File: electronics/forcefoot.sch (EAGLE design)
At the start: 60 parts

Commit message: Tying AGND to GND
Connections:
- removed net AGND$1: C2.1, HX1.AGND, R17.1
- removed net AGND$2: C6.1, HX2.AGND, R5.1
- removed net AGND$3: C10.1, HX3.AGND, R8.1
- removed net AGND$4: C14.1, HX4.AGND, R11.1
- net GND: now also C10.1, C14.1, C2.1, C6.1, HX1.AGND, HX2.AGND, HX3.AGND, HX4.AGND, R11.1, R17.1, R5.1, R8.1
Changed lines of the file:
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@@
 <part name="GND7" library="supply1" deviceset="GND" device=""/>
 <part name="GND8" library="supply1" deviceset="GND" device=""/>
+<part name="GND9" library="supply1" deviceset="GND" device=""/>
+<part name="GND10" library="supply1" deviceset="GND" device=""/>
+<part name="GND12" library="supply1" deviceset="GND" device=""/>
+<part name="GND13" library="supply1" deviceset="GND" device=""/>
 </parts>
 <sheets>
@@
 <instance part="GND7" gate="1" x="190.5" y="132.08"/>
 <instance part="GND8" gate="1" x="200.66" y="132.08"/>
+<instance part="GND9" gate="1" x="25.4" y="30.48"/>
+<instance part="GND10" gate="1" x="144.78" y="27.94"/>
+<instance part="GND12" gate="1" x="264.16" y="27.94"/>
+<instance part="GND13" gate="1" x="378.46" y="27.94"/>
 </instances>
 <busses>
@@
 <pinref part="U$4" gate="G$1" pin="-"/>
 <wire x1="200.66" y1="137.16" x2="200.66" y2="134.62" width="0.1524" layer="91"/>
+</segment>
+<segment>
+<pinref part="C2" gate="G$1" pin="1"/>
+<wire x1="45.72" y1="53.34" x2="43.18" y2="53.34" width="0.1524" layer="91"/>
+<wire x1="43.18" y1="33.02" x2="43.18" y2="53.34" width="0.1524" layer="91"/>
+<wire x1="43.18" y1="53.34" x2="43.18" y2="58.42" width="0.1524" layer="91"/>
+<pinref part="HX1" gate="G$1" pin="AGND"/>
+<wire x1="43.18" y1="58.42" x2="55.88" y2="58.42" width="0.1524" layer="91"/>
+<pinref part="R17" gate="G$1" pin="1"/>
+<wire x1="25.4" y1="35.56" x2="25.4" y2="33.02" width="0.1524" layer="91"/>
+<wire x1="25.4" y1="33.02" x2="43.18" y2="33.02" width="0.1524" layer="91"/>
+<junction x="25.4" y="33.02"/>
+<junction x="43.18" y="33.02"/>
+<junction x="43.18" y="53.34"/>
+<pinref part="GND9" gate="1" pin="GND"/>
+</segment>
+<segment>
+<pinref part="R5" gate="G$1" pin="1"/>
+<wire x1="144.78" y1="33.02" x2="144.78" y2="30.48" width="0.1524" layer="91"/>
+<pinref part="C6" gate="G$1" pin="1"/>
+<wire x1="165.1" y1="50.8" x2="162.56" y2="50.8" width="0.1524" layer="91"/>
+<wire x1="144.78" y1="30.48" x2="162.56" y2="30.48" width="0.1524" layer="91"/>
+<wire x1="162.56" y1="30.48" x2="162.56" y2="50.8" width="0.1524" layer="91"/>
+<wire x1="162.56" y1="50.8" x2="162.56" y2="55.88" width="0.1524" layer="91"/>
+<pinref part="HX2" gate="G$1" pin="AGND"/>
+<wire x1="162.56" y1="55.88" x2="175.26" y2="55.88" width="0.1524" layer="91"/>
+<junction x="162.56" y="50.8"/>
+<pinref part="GND10" gate="1" pin="GND"/>
+<junction x="144.78" y="30.48"/>
+</segment>
+<segment>
+<pinref part="R8" gate="G$1" pin="1"/>
+<wire x1="264.16" y1="33.02" x2="264.16" y2="30.48" width="0.1524" layer="91"/>
+<pinref part="C10" gate="G$1" pin="1"/>
+<wire x1="284.48" y1="50.8" x2="281.94" y2="50.8" width="0.1524" layer="91"/>
+<wire x1="264.16" y1="30.48" x2="281.94" y2="30.48" width="0.1524" layer="91"/>
+<wire x1="281.94" y1="30.48" x2="281.94" y2="50.8" width="0.1524" layer="91"/>
+<wire x1="281.94" y1="50.8" x2="281.94" y2="55.88" width="0.1524" layer="91"/>
+<pinref part="HX3" gate="G$1" pin="AGND"/>
+<wire x1="281.94" y1="55.88" x2="294.64" y2="55.88" width="0.1524" layer="91"/>
+<junction x="281.94" y="50.8"/>
+<pinref part="GND12" gate="1" pin="GND"/>
+<junction x="264.16" y="30.48"/>
+</segment>
+<segment>
+<pinref part="R11" gate="G$1" pin="1"/>
+<wire x1="378.46" y1="33.02" x2="378.46" y2="30.48" width="0.1524" layer="91"/>
+<pinref part="C14" gate="G$1" pin="1"/>
+<wire x1="398.78" y1="50.8" x2="396.24" y2="50.8" width="0.1524" layer="91"/>
+<wire x1="378.46" y1="30.48" x2="396.24" y2="30.48" width="0.1524" layer="91"/>
+<wire x1="396.24" y1="30.48" x2="396.24" y2="50.8" width="0.1524" layer="91"/>
+<wire x1="396.24" y1="50.8" x2="396.24" y2="55.88" width="0.1524" layer="91"/>
+<pinref part="HX4" gate="G$1" pin="AGND"/>
+<wire x1="396.24" y1="55.88" x2="408.94" y2="55.88" width="0.1524" layer="91"/>
+<junction x="396.24" y="50.8"/>
+<pinref part="GND13" gate="1" pin="GND"/>
+<junction x="378.46" y="30.48"/>
 </segment>
 </net>
@@
 </segment>
 </net>
-<net name="AGND$1" class="0">
-<segment>
-<pinref part="C2" gate="G$1" pin="1"/>
-<wire x1="45.72" y1="53.34" x2="43.18" y2="53.34" width="0.1524" layer="91"/>
-<wire x1="43.18" y1="33.02" x2="43.18" y2="53.34" width="0.1524" layer="91"/>
-<wire x1="43.18" y1="53.34" x2="43.18" y2="58.42" width="0.1524" layer="91"/>
-<pinref part="HX1" gate="G$1" pin="AGND"/>
-<wire x1="43.18" y1="58.42" x2="55.88" y2="58.42" width="0.1524" layer="91"/>
-<pinref part="R17" gate="G$1" pin="1"/>
-<wire x1="25.4" y1="35.56" x2="25.4" y2="33.02" width="0.1524" layer="91"/>
-<wire x1="25.4" y1="33.02" x2="43.18" y2="33.02" width="0.1524" layer="91"/>
-<junction x="25.4" y="33.02"/>
-<junction x="43.18" y="33.02"/>
-<junction x="43.18" y="53.34"/>
-</segment>
-</net>
 <net name="N$3" class="0">
 <segment>
@@
 </segment>
 </net>
-<net name="AGND$2" class="0">
-<segment>
-<pinref part="R5" gate="G$1" pin="1"/>
-<wire x1="144.78" y1="33.02" x2="144.78" y2="30.48" width="0.1524" layer="91"/>
-<pinref part="C6" gate="G$1" pin="1"/>
-<wire x1="165.1" y1="50.8" x2="162.56" y2="50.8" width="0.1524" layer="91"/>
-<wire x1="144.78" y1="30.48" x2="162.56" y2="30.48" width="0.1524" layer="91"/>
-<wire x1="162.56" y1="30.48" x2="162.56" y2="50.8" width="0.1524" layer="91"/>
-<wire x1="162.56" y1="50.8" x2="162.56" y2="55.88" width="0.1524" layer="91"/>
-<pinref part="HX2" gate="G$1" pin="AGND"/>
-<wire x1="162.56" y1="55.88" x2="175.26" y2="55.88" width="0.1524" layer="91"/>
-<junction x="162.56" y="50.8"/>
-</segment>
-</net>
 <net name="N$4" class="0">
 <segment>
@@
 </segment>
 </net>
-<net name="AGND$3" class="0">
-<segment>
-<pinref part="R8" gate="G$1" pin="1"/>
-<wire x1="264.16" y1="33.02" x2="264.16" y2="30.48" width="0.1524" layer="91"/>
-<pinref part="C10" gate="G$1" pin="1"/>
-<wire x1="284.48" y1="50.8" x2="281.94" y2="50.8" width="0.1524" layer="91"/>
-<wire x1="264.16" y1="30.48" x2="281.94" y2="30.48" width="0.1524" layer="91"/>
-<wire x1="281.94" y1="30.48" x2="281.94" y2="50.8" width="0.1524" layer="91"/>
-<wire x1="281.94" y1="50.8" x2="281.94" y2="55.88" width="0.1524" layer="91"/>
-<pinref part="HX3" gate="G$1" pin="AGND"/>
-<wire x1="281.94" y1="55.88" x2="294.64" y2="55.88" width="0.1524" layer="91"/>
-<junction x="281.94" y="50.8"/>
-</segment>
-</net>
 <net name="N$6" class="0">
 <segment>
@@
 </segment>
 </net>
-<net name="AGND$4" class="0">
-<segment>
-<pinref part="R11" gate="G$1" pin="1"/>
-<wire x1="378.46" y1="33.02" x2="378.46" y2="30.48" width="0.1524" layer="91"/>
-<pinref part="C14" gate="G$1" pin="1"/>
-<wire x1="398.78" y1="50.8" x2="396.24" y2="50.8" width="0.1524" layer="91"/>
-<wire x1="378.46" y1="30.48" x2="396.24" y2="30.48" width="0.1524" layer="91"/>
-<wire x1="396.24" y1="30.48" x2="396.24" y2="50.8" width="0.1524" layer="91"/>
-<wire x1="396.24" y1="50.8" x2="396.24" y2="55.88" width="0.1524" layer="91"/>
-<pinref part="HX4" gate="G$1" pin="AGND"/>
-<wire x1="396.24" y1="55.88" x2="408.94" y2="55.88" width="0.1524" layer="91"/>
-<junction x="396.24" y="50.8"/>
-</segment>
-</net>

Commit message: Tweaking for v2
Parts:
- removed DXL: CONNEC_1X04, rhoban:CONNEC_1X04
- removed IC1: (no value), SparkFun-PowerIC:V_REG_78XX-TO-220
- removed MAPLE_MINI: MAPLE_MINI, rhoban:MAPLE_MINI
- added C17, C18: 22, rhoban:C_EU_22PF
- added R27: 10k, SparkFun-Passives:RESISTOR0805-RES
- added R28, R29: 3K, SparkFun-Passives:RESISTOR0805-RES
- added U$17: GY-85, rhoban:GY-85
- added U$28: CONNEC_2X03, rhoban:CONNEC_2X03
- added U$5: REG_5V, rhoban:REG_5V
- added U$8: CONNEC_1X04_485, rhoban:CONNEC_1X04_485
- added U2: ATMEGA168, SparkFun-DigitalIC:ATMEGA168
- added XTAL1: QUARTZ, rhoban:QUARTZ
- U$10, U$13, U$3, U$7: value CONNEC_1X04 -> CONNEC_1X041.5; device rhoban:CONNEC_1X04 -> rhoban:CONNEC_1X041.5
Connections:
- new net 3.3: R28.2, R29.2, U$17.3.3
- new net IMU_SCL: R28.1, U$17.SCL, U2.PC5(ADC5/SCL)
- new net IMU_SDA: R29.1, U$17.SDA, U2.PC4(ADC4/SDA)
- new net MISO: U$28.1, U2.PB4(MISO)
- new net MOSI: U$28.4, U2.PB3(MOSI/OC2)
- new net N$19: C17.2, U2.PB6(XTAL1/TOSC1), XTAL1.2
- new net N$20: C18.2, U2.PB7(XTAL2/TOSC2), XTAL1.1
- new net RESET: R27.1, U$28.5, U2.PC6(/RESET)
- new net SCK: U$28.3, U2.PB5(SCK)
- net DIRECTION: now also U2.PD2(INT0); no longer MAPLE_MINI.2
- net DOUT1: now also U2.PC1(ADC1); no longer MAPLE_MINI.16
- net DOUT2: now also U2.PC3(ADC3); no longer MAPLE_MINI.18
- net DOUT3: now also U2.PD4(XCK/T0); no longer MAPLE_MINI.20
- net DOUT4: now also U2.ADC7; no longer MAPLE_MINI.22
- net GND: now also C17.1, C18.1, U$17.GND, U$28.6, U$5.GND, U$8.1, U2.AGND, U2.GND@1, U2.GND@2; no longer DXL.1, IC1.GND, MAPLE_MINI.GND
- net RS+: now also U$8.3; no longer DXL.3
- net RS-: now also U$8.4; no longer DXL.4
- net RX: now also U2.PD0(RXD); no longer MAPLE_MINI.0
- net SCK1: now also U2.PC0(ADC0); no longer MAPLE_MINI.15
- net SCK2: now also U2.PC2(ADC2); no longer MAPLE_MINI.17
- net SCK3: now also U2.PD3(INT1); no longer MAPLE_MINI.19
- net SCK4: now also U2.ADC6; no longer MAPLE_MINI.21
- net TX: now also U2.PD1(TXD); no longer MAPLE_MINI.1
- net VCC: now also U$17.VCC_IN, U$5.OUT; no longer IC1.OUT, MAPLE_MINI.VIN
- net VIN: now also R27.2, U$28.2, U$5.IN, U$8.2, U2.AREF, U2.VCC@1, U2.VCC@2; no longer DXL.2, IC1.IN
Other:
- moved on the sheet: MAX485, R1, R13, R14, R15, R18, R2, U$2, U$4

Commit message: Fixing r value
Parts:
- R14, R15: value 3k -> 22
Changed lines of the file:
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@@
 <part name="GND2" library="supply1" deviceset="GND" device=""/>
 <part name="P+1" library="supply1" deviceset="VCC" device=""/>
-<part name="R14" library="rhoban" deviceset="RESISTANCE" device="-R0805" value="3k"/>
-<part name="R15" library="rhoban" deviceset="RESISTANCE" device="-R0805" value="3k"/>
+<part name="R14" library="rhoban" deviceset="RESISTANCE" device="-R0805" value="22"/>
+<part name="R15" library="rhoban" deviceset="RESISTANCE" device="-R0805" value="22"/>
 <part name="R19" library="SparkFun-Passives" deviceset="RESISTOR" device="0805-RES" value="3K"/>
 <part name="R20" library="SparkFun-Passives" deviceset="RESISTOR" device="0805-RES" value="3K"/>

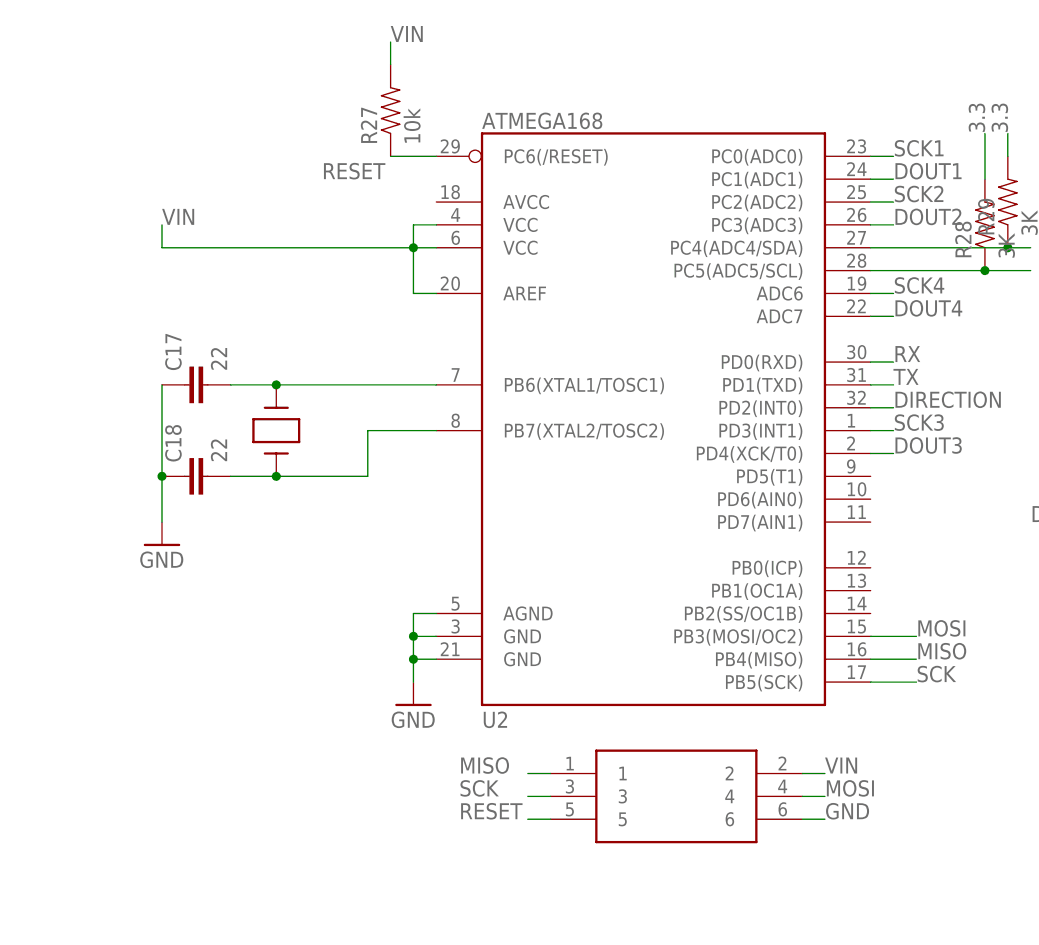
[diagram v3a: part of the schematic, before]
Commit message: Fixing vin -> vcc for mcu
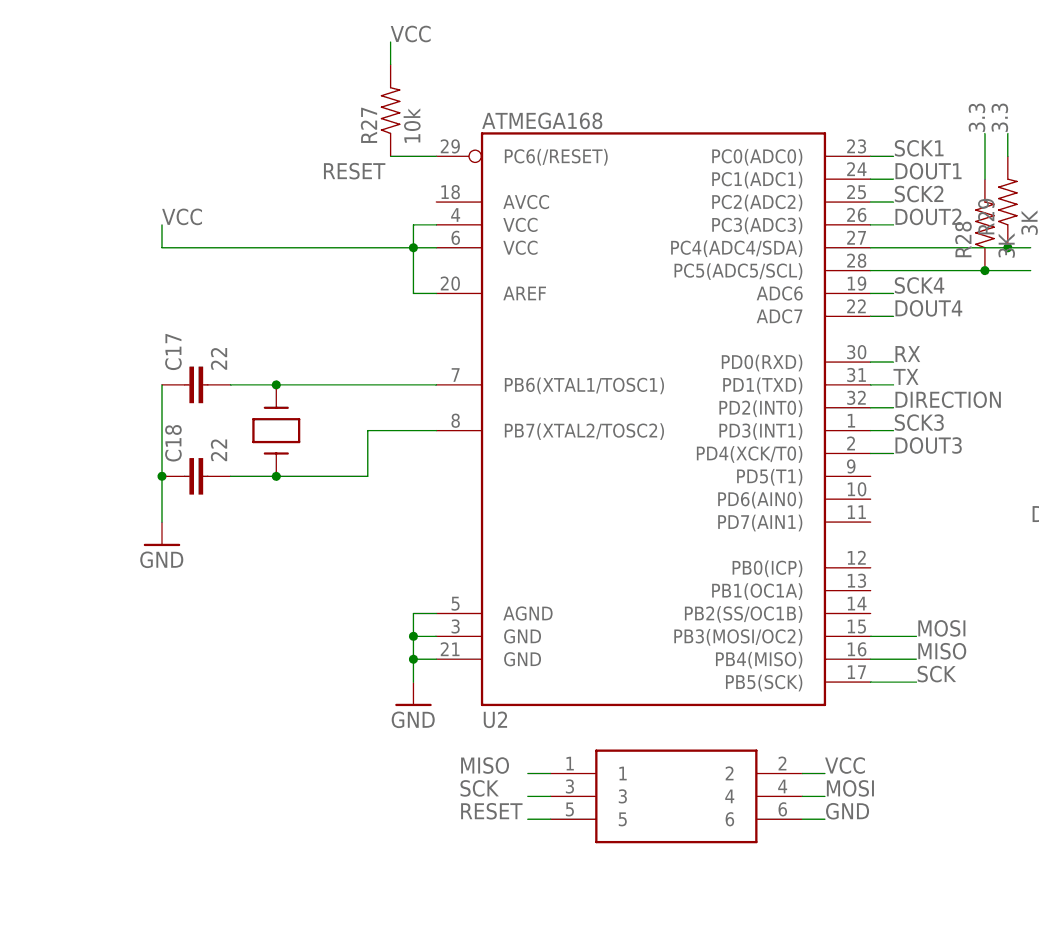
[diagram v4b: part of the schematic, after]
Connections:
- net VCC: now also R27.2, U$28.2, U2.AREF, U2.VCC@1, U2.VCC@2
- net VIN: no longer R27.2, U$28.2, U2.AREF, U2.VCC@1, U2.VCC@2
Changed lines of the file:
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@@
 <label x="226.06" y="187.96" size="1.778" layer="95"/>
+</segment>
+<segment>
+<wire x1="119.38" y1="167.64" x2="119.38" y2="165.1" width="0.1524" layer="91"/>
+<wire x1="119.38" y1="165.1" x2="147.32" y2="165.1" width="0.1524" layer="91"/>
+<wire x1="147.32" y1="165.1" x2="149.86" y2="165.1" width="0.1524" layer="91"/>
+<wire x1="149.86" y1="167.64" x2="147.32" y2="167.64" width="0.1524" layer="91"/>
+<wire x1="147.32" y1="167.64" x2="147.32" y2="165.1" width="0.1524" layer="91"/>
+<junction x="147.32" y="165.1"/>
+<wire x1="149.86" y1="160.02" x2="147.32" y2="160.02" width="0.1524" layer="91"/>
+<wire x1="147.32" y1="160.02" x2="147.32" y2="165.1" width="0.1524" layer="91"/>
+<label x="119.38" y="167.64" size="1.778" layer="95"/>
+<pinref part="U2" gate="G$1" pin="VCC@1"/>
+<pinref part="U2" gate="G$1" pin="VCC@2"/>
+<pinref part="U2" gate="G$1" pin="AREF"/>
+</segment>
+<segment>
+<pinref part="U$28" gate="G$1" pin="2"/>
+<wire x1="190.5" y1="106.68" x2="193.04" y2="106.68" width="0.1524" layer="91"/>
+<label x="193.04" y="106.68" size="1.778" layer="95"/>
+</segment>
+<segment>
+<wire x1="144.78" y1="187.96" x2="144.78" y2="185.42" width="0.1524" layer="91"/>
+<pinref part="R27" gate="G$1" pin="2"/>
+<label x="144.78" y="187.96" size="1.778" layer="95"/>
 </segment>
 </net>
@@
 </segment>
 <segment>
-<pinref part="U$28" gate="G$1" pin="2"/>
-<wire x1="190.5" y1="106.68" x2="193.04" y2="106.68" width="0.1524" layer="91"/>
-<label x="193.04" y="106.68" size="1.778" layer="95"/>
-</segment>
-<segment>
-<wire x1="119.38" y1="167.64" x2="119.38" y2="165.1" width="0.1524" layer="91"/>
-<wire x1="119.38" y1="165.1" x2="147.32" y2="165.1" width="0.1524" layer="91"/>
-<wire x1="147.32" y1="165.1" x2="149.86" y2="165.1" width="0.1524" layer="91"/>
-<wire x1="149.86" y1="167.64" x2="147.32" y2="167.64" width="0.1524" layer="91"/>
-<wire x1="147.32" y1="167.64" x2="147.32" y2="165.1" width="0.1524" layer="91"/>
-<junction x="147.32" y="165.1"/>
-<wire x1="149.86" y1="160.02" x2="147.32" y2="160.02" width="0.1524" layer="91"/>
-<wire x1="147.32" y1="160.02" x2="147.32" y2="165.1" width="0.1524" layer="91"/>
-<label x="119.38" y="167.64" size="1.778" layer="95"/>
-<pinref part="U2" gate="G$1" pin="VCC@1"/>
-<pinref part="U2" gate="G$1" pin="VCC@2"/>
-<pinref part="U2" gate="G$1" pin="AREF"/>
-</segment>
-<segment>
-<wire x1="144.78" y1="187.96" x2="144.78" y2="185.42" width="0.1524" layer="91"/>
-<pinref part="R27" gate="G$1" pin="2"/>
-<label x="144.78" y="187.96" size="1.778" layer="95"/>
-</segment>
-<segment>

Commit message: Fixing connections
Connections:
- removed net 1A-1: R21.1, R22.2
- removed net 1A-2: R23.1, R24.2
- removed net 1A-3: R25.1, R26.2
- net 2A-: now also R21.1, R22.2
- net 3A-: now also R23.1, R24.2
- net 4A-: now also R25.1, R26.2
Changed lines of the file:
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@@
 <junction x="165.1" y="25.4"/>
+</segment>
+<segment>
+<wire x1="144.78" y1="25.4" x2="127" y2="25.4" width="0.1524" layer="91"/>
+<pinref part="R21" gate="G$1" pin="1"/>
+<pinref part="R22" gate="G$1" pin="2"/>
+<junction x="127" y="25.4"/>
 </segment>
 </net>
@@
 <junction x="398.78" y="25.4"/>
 </segment>
+<segment>
+<wire x1="378.46" y1="25.4" x2="360.68" y2="25.4" width="0.1524" layer="91"/>
+<pinref part="R25" gate="G$1" pin="1"/>
+<pinref part="R26" gate="G$1" pin="2"/>
+<junction x="360.68" y="25.4"/>
+</segment>
 </net>
 <net name="3A-" class="0">
@@
 <wire x1="264.16" y1="15.24" x2="264.16" y2="25.4" width="0.1524" layer="91"/>
 <junction x="284.48" y="25.4"/>
+</segment>
+<segment>
+<wire x1="264.16" y1="25.4" x2="246.38" y2="25.4" width="0.1524" layer="91"/>
+<pinref part="R23" gate="G$1" pin="1"/>
+<pinref part="R24" gate="G$1" pin="2"/>
+<junction x="246.38" y="25.4"/>
 </segment>
 </net>
@@
 </segment>
 </net>
-<net name="1A-1" class="0">
-<segment>
-<wire x1="144.78" y1="25.4" x2="127" y2="25.4" width="0.1524" layer="91"/>
-<pinref part="R21" gate="G$1" pin="1"/>
-<pinref part="R22" gate="G$1" pin="2"/>
-<junction x="127" y="25.4"/>
-</segment>
-</net>
-<net name="1A-2" class="0">
-<segment>
-<wire x1="264.16" y1="25.4" x2="246.38" y2="25.4" width="0.1524" layer="91"/>
-<pinref part="R23" gate="G$1" pin="1"/>
-<pinref part="R24" gate="G$1" pin="2"/>
-<junction x="246.38" y="25.4"/>
-</segment>
-</net>
-<net name="1A-3" class="0">
-<segment>
-<wire x1="378.46" y1="25.4" x2="360.68" y2="25.4" width="0.1524" layer="91"/>
-<pinref part="R25" gate="G$1" pin="1"/>
-<pinref part="R26" gate="G$1" pin="2"/>
-<junction x="360.68" y="25.4"/>
-</segment>
-</net>

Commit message: Improving names and silk
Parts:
- removed U$17: GY-85, rhoban:GY-85
- removed U$28: CONNEC_2X03, rhoban:CONNEC_2X03
- removed U$5: REG_5V, rhoban:REG_5V
- removed U$8: CONNEC_1X04_485, rhoban:CONNEC_1X04_485
- added DXL: CONNEC_1X04_485, rhoban:CONNEC_1X04_485
- added IMU: GY-85, rhoban:GY-85
- added ISP: CONNEC_2X03, rhoban:CONNEC_2X03
- added REG: REG_5V, rhoban:REG_5V
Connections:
- net 3.3: now also IMU.3.3; no longer U$17.3.3
- net GND: now also DXL.1, IMU.GND, ISP.6, REG.GND; no longer U$17.GND, U$28.6, U$5.GND, U$8.1
- net IMU_SCL: now also IMU.SCL; no longer U$17.SCL
- net IMU_SDA: now also IMU.SDA; no longer U$17.SDA
- net MISO: now also ISP.1; no longer U$28.1
- net MOSI: now also ISP.4; no longer U$28.4
- net RESET: now also ISP.5; no longer U$28.5
- net RS+: now also DXL.3; no longer U$8.3
- net RS-: now also DXL.4; no longer U$8.4
- net SCK: now also ISP.3; no longer U$28.3
- net VCC: now also IMU.VCC_IN, ISP.2, REG.OUT; no longer U$17.VCC_IN, U$28.2, U$5.OUT
- net VIN: now also DXL.2, REG.IN; no longer U$5.IN, U$8.2
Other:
- moved on the sheet: C17, C18, MAX485, R1, R13, R14, R15, R18, R2, R27, R28, R29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

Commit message: Adding FARNELL attributes and writing BOM
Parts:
- C1, C10, C11, C13, C14, C15, C2, C3, C5, C6, C7, C9: FARNELL (none) -> 2525136RL
- C12, C16, C4, C8: FARNELL (none) -> 2688486RL
- C17, C18: FARNELL (none) -> 1759489RL
- DXL: FARNELL (none) -> 1104204 OR 9979620
- HX1, HX2, HX3, HX4: FARNELL (none) -> HX711
- IMU: FARNELL (none) -> -
- ISP: FARNELL (none) -> 1593440
- MAX485: FARNELL (none) -> 1564306
- R1, R13, R18, R19, R2, R20, R21, R22, R23, R24, R25, R26, R28, R29: FARNELL (none) -> 2074431
- R10, R16, R4, R7: FARNELL (none) -> 2074395
- R11, R17, R5, R8: FARNELL (none) -> 2074518
- R12, R3, R6, R9: FARNELL (none) -> 2074332RL
- R14, R15: FARNELL (none) -> 2446926
- R27: FARNELL (none) -> 2074334RL
- REG: FARNELL (none) -> 1696320
- U$1, U$12, U$6, U$9: FARNELL (none) -> 1095136
- U$10, U$13, U$3, U$7: FARNELL (none) -> 9491791
- U$2: FARNELL (none) -> 9696946
- U$4: FARNELL (none) -> 1850103
- U2: FARNELL (none) -> 2523203
- XTAL1: FARNELL (none) -> 7940506
